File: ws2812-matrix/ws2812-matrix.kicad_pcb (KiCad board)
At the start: 2 copper layers, 80 x 80 mm, 270 parts, among them J1 Conn_01x03, J2 Conn_01x03

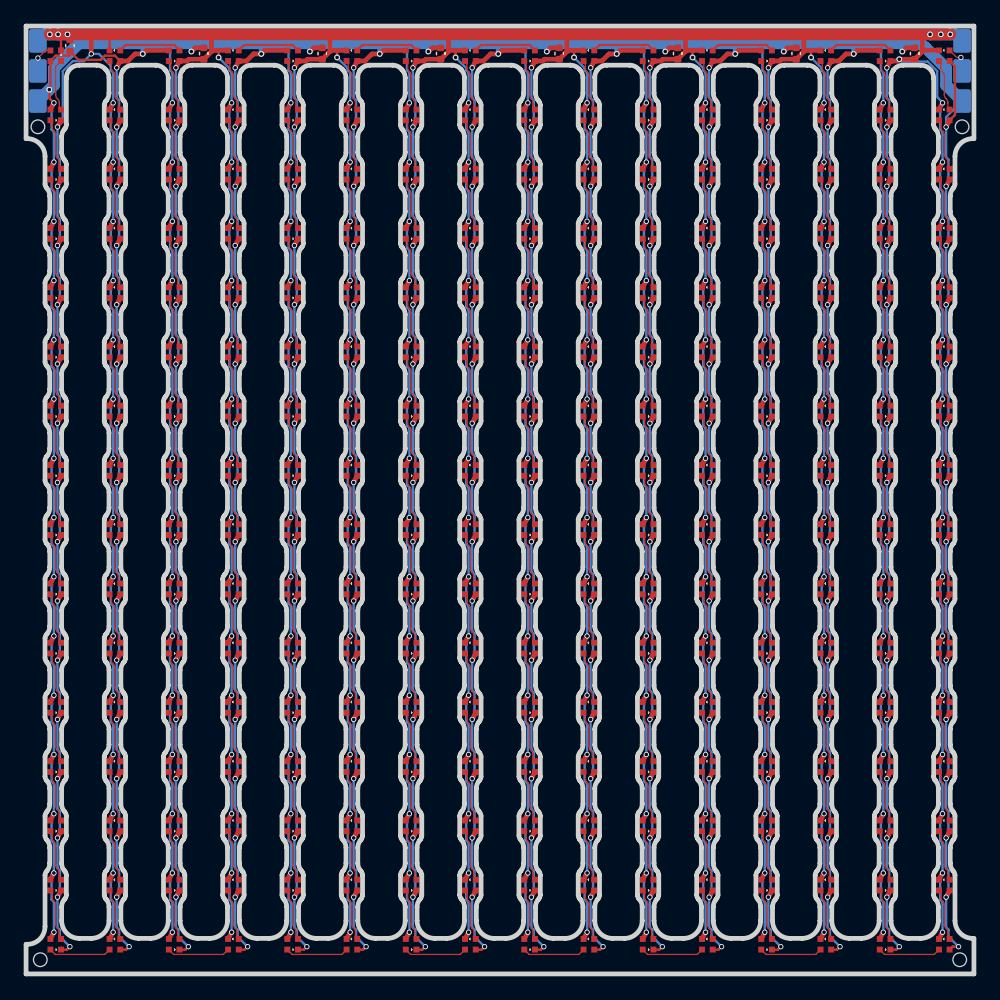
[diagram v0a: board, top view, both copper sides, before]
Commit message: ws2812-matrix: new attempt with more connections
Hopefully this'll go through JLCPCB review.
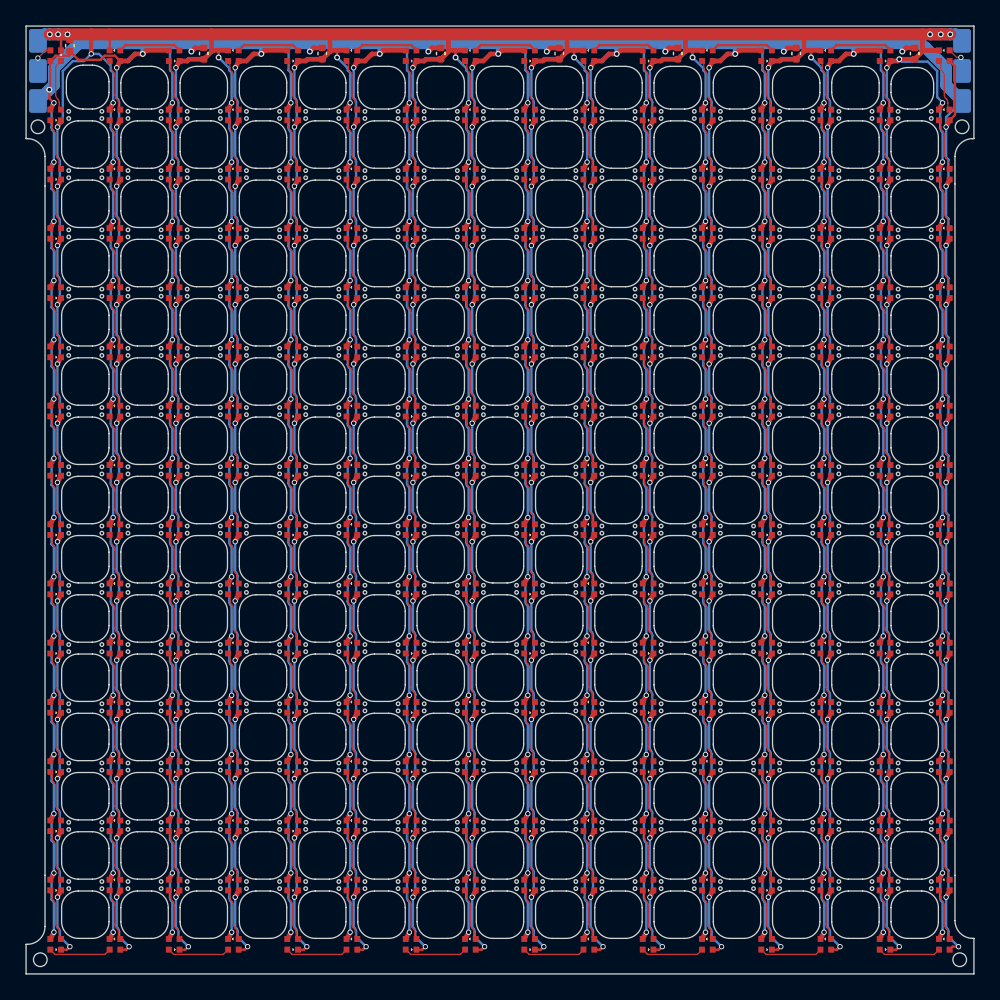
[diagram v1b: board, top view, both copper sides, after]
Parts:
- added REF**: BreakawayHole, Custom:BreakawayHole, F.Cu at (51.1, 54.7)
- added REF**: BreakawayHole, Custom:BreakawayHole, F.Cu at (51.1, 55.3)
- added REF**: BreakawayHole, Custom:BreakawayHole, F.Cu at (53.9, 55.3)
- added REF**: BreakawayHole, Custom:BreakawayHole, F.Cu at (51.1, 60.3)
- added REF**: BreakawayHole, Custom:BreakawayHole, F.Cu at (53.9, 54.7)
- added REF**: BreakawayHole, Custom:BreakawayHole, F.Cu at (53.9, 60.3)
- added REF**: BreakawayHole, Custom:BreakawayHole, F.Cu at (51.1, 59.7)
- added REF**: BreakawayHole, Custom:BreakawayHole, F.Cu at (53.9, 59.7)
- added REF**1: BreakawayHole, Custom:BreakawayHole, F.Cu at (56.1, 60.3)
- added REF**10: BreakawayHole, Custom:BreakawayHole, F.Cu at (76.1, 59.7)
- added REF**100: BreakawayHole, Custom:BreakawayHole, F.Cu at (76.1, 74.7)
- added REF**101: BreakawayHole, Custom:BreakawayHole, F.Cu at (81.1, 75.3)
- added REF**102: BreakawayHole, Custom:BreakawayHole, F.Cu at (81.1, 74.7)
- added REF**103: BreakawayHole, Custom:BreakawayHole, F.Cu at (86.1, 75.3)
- added REF**104: BreakawayHole, Custom:BreakawayHole, F.Cu at (86.1, 74.7)
- added REF**105: BreakawayHole, Custom:BreakawayHole, F.Cu at (91.1, 75.3)
- added REF**106: BreakawayHole, Custom:BreakawayHole, F.Cu at (91.1, 74.7)
- added REF**107: BreakawayHole, Custom:BreakawayHole, F.Cu at (96.1, 75.3)
- added REF**108: BreakawayHole, Custom:BreakawayHole, F.Cu at (96.1, 74.7)
- added REF**109: BreakawayHole, Custom:BreakawayHole, F.Cu at (101.1, 75.3)
- added REF**11: BreakawayHole, Custom:BreakawayHole, F.Cu at (81.1, 60.3)
- added REF**110: BreakawayHole, Custom:BreakawayHole, F.Cu at (101.1, 74.7)
- added REF**111: BreakawayHole, Custom:BreakawayHole, F.Cu at (106.1, 75.3)
- added REF**112: BreakawayHole, Custom:BreakawayHole, F.Cu at (106.1, 74.7)
- added REF**113: BreakawayHole, Custom:BreakawayHole, F.Cu at (111.1, 75.3)
- added REF**114: BreakawayHole, Custom:BreakawayHole, F.Cu at (111.1, 74.7)
- added REF**115: BreakawayHole, Custom:BreakawayHole, F.Cu at (116.1, 75.3)
- added REF**116: BreakawayHole, Custom:BreakawayHole, F.Cu at (116.1, 74.7)
- added REF**117: BreakawayHole, Custom:BreakawayHole, F.Cu at (121.1, 75.3)
- added REF**118: BreakawayHole, Custom:BreakawayHole, F.Cu at (121.1, 74.7)
- added REF**119: BreakawayHole, Custom:BreakawayHole, F.Cu at (51.1, 80.3)
- added REF**12: BreakawayHole, Custom:BreakawayHole, F.Cu at (81.1, 59.7)
- added REF**120: BreakawayHole, Custom:BreakawayHole, F.Cu at (51.1, 79.7)
- added REF**121: BreakawayHole, Custom:BreakawayHole, F.Cu at (56.1, 80.3)
- added REF**122: BreakawayHole, Custom:BreakawayHole, F.Cu at (56.1, 79.7)
- added REF**123: BreakawayHole, Custom:BreakawayHole, F.Cu at (61.1, 80.3)
- added REF**124: BreakawayHole, Custom:BreakawayHole, F.Cu at (61.1, 79.7)
- added REF**125: BreakawayHole, Custom:BreakawayHole, F.Cu at (66.1, 80.3)
- added REF**126: BreakawayHole, Custom:BreakawayHole, F.Cu at (66.1, 79.7)
- added REF**127: BreakawayHole, Custom:BreakawayHole, F.Cu at (71.1, 80.3)
- added REF**128: BreakawayHole, Custom:BreakawayHole, F.Cu at (71.1, 79.7)
- added REF**129: BreakawayHole, Custom:BreakawayHole, F.Cu at (76.1, 80.3)
- added REF**13: BreakawayHole, Custom:BreakawayHole, F.Cu at (86.1, 60.3)
- added REF**130: BreakawayHole, Custom:BreakawayHole, F.Cu at (76.1, 79.7)
- added REF**131: BreakawayHole, Custom:BreakawayHole, F.Cu at (81.1, 80.3)
- added REF**132: BreakawayHole, Custom:BreakawayHole, F.Cu at (81.1, 79.7)
- added REF**133: BreakawayHole, Custom:BreakawayHole, F.Cu at (86.1, 80.3)
- added REF**134: BreakawayHole, Custom:BreakawayHole, F.Cu at (86.1, 79.7)
- added REF**135: BreakawayHole, Custom:BreakawayHole, F.Cu at (91.1, 80.3)
- added REF**136: BreakawayHole, Custom:BreakawayHole, F.Cu at (91.1, 79.7)
- added REF**137: BreakawayHole, Custom:BreakawayHole, F.Cu at (96.1, 80.3)
- added REF**138: BreakawayHole, Custom:BreakawayHole, F.Cu at (96.1, 79.7)
- added REF**139: BreakawayHole, Custom:BreakawayHole, F.Cu at (101.1, 80.3)
- added REF**14: BreakawayHole, Custom:BreakawayHole, F.Cu at (86.1, 59.7)
- added REF**140: BreakawayHole, Custom:BreakawayHole, F.Cu at (101.1, 79.7)
- added REF**141: BreakawayHole, Custom:BreakawayHole, F.Cu at (106.1, 80.3)
- added REF**142: BreakawayHole, Custom:BreakawayHole, F.Cu at (106.1, 79.7)
- added REF**143: BreakawayHole, Custom:BreakawayHole, F.Cu at (111.1, 80.3)
- added REF**144: BreakawayHole, Custom:BreakawayHole, F.Cu at (111.1, 79.7)
- added REF**145: BreakawayHole, Custom:BreakawayHole, F.Cu at (116.1, 80.3)
- added REF**146: BreakawayHole, Custom:BreakawayHole, F.Cu at (116.1, 79.7)
- added REF**147: BreakawayHole, Custom:BreakawayHole, F.Cu at (121.1, 80.3)
- added REF**148: BreakawayHole, Custom:BreakawayHole, F.Cu at (121.1, 79.7)
- added REF**149: BreakawayHole, Custom:BreakawayHole, F.Cu at (51.1, 85.3)
- added REF**15: BreakawayHole, Custom:BreakawayHole, F.Cu at (91.1, 60.3)
- added REF**150: BreakawayHole, Custom:BreakawayHole, F.Cu at (51.1, 84.7)
- added REF**151: BreakawayHole, Custom:BreakawayHole, F.Cu at (56.1, 85.3)
- added REF**152: BreakawayHole, Custom:BreakawayHole, F.Cu at (56.1, 84.7)
- added REF**153: BreakawayHole, Custom:BreakawayHole, F.Cu at (61.1, 85.3)
- added REF**154: BreakawayHole, Custom:BreakawayHole, F.Cu at (61.1, 84.7)
- added REF**155: BreakawayHole, Custom:BreakawayHole, F.Cu at (66.1, 85.3)
- added REF**156: BreakawayHole, Custom:BreakawayHole, F.Cu at (66.1, 84.7)
- added REF**157: BreakawayHole, Custom:BreakawayHole, F.Cu at (71.1, 85.3)
- added REF**158: BreakawayHole, Custom:BreakawayHole, F.Cu at (71.1, 84.7)
- added REF**159: BreakawayHole, Custom:BreakawayHole, F.Cu at (76.1, 85.3)
- added REF**16: BreakawayHole, Custom:BreakawayHole, F.Cu at (91.1, 59.7)
- added REF**160: BreakawayHole, Custom:BreakawayHole, F.Cu at (76.1, 84.7)
- added REF**161: BreakawayHole, Custom:BreakawayHole, F.Cu at (81.1, 85.3)
- added REF**162: BreakawayHole, Custom:BreakawayHole, F.Cu at (81.1, 84.7)
- added REF**163: BreakawayHole, Custom:BreakawayHole, F.Cu at (86.1, 85.3)
- added REF**164: BreakawayHole, Custom:BreakawayHole, F.Cu at (86.1, 84.7)
- added REF**165: BreakawayHole, Custom:BreakawayHole, F.Cu at (91.1, 85.3)
- added REF**166: BreakawayHole, Custom:BreakawayHole, F.Cu at (91.1, 84.7)
- added REF**167: BreakawayHole, Custom:BreakawayHole, F.Cu at (96.1, 85.3)
- added REF**168: BreakawayHole, Custom:BreakawayHole, F.Cu at (96.1, 84.7)
- added REF**169: BreakawayHole, Custom:BreakawayHole, F.Cu at (101.1, 85.3)
- added REF**17: BreakawayHole, Custom:BreakawayHole, F.Cu at (96.1, 60.3)
- added REF**170: BreakawayHole, Custom:BreakawayHole, F.Cu at (101.1, 84.7)
- added REF**171: BreakawayHole, Custom:BreakawayHole, F.Cu at (106.1, 85.3)
- added REF**172: BreakawayHole, Custom:BreakawayHole, F.Cu at (106.1, 84.7)
- added REF**173: BreakawayHole, Custom:BreakawayHole, F.Cu at (111.1, 85.3)
- added REF**174: BreakawayHole, Custom:BreakawayHole, F.Cu at (111.1, 84.7)
- added REF**175: BreakawayHole, Custom:BreakawayHole, F.Cu at (116.1, 85.3)
- added REF**176: BreakawayHole, Custom:BreakawayHole, F.Cu at (116.1, 84.7)
- added REF**177: BreakawayHole, Custom:BreakawayHole, F.Cu at (121.1, 85.3)
- added REF**178: BreakawayHole, Custom:BreakawayHole, F.Cu at (121.1, 84.7)
- added REF**179: BreakawayHole, Custom:BreakawayHole, F.Cu at (51.1, 90.3)
- added REF**18: BreakawayHole, Custom:BreakawayHole, F.Cu at (96.1, 59.7)
- added REF**180: BreakawayHole, Custom:BreakawayHole, F.Cu at (51.1, 89.7)
- added REF**181: BreakawayHole, Custom:BreakawayHole, F.Cu at (56.1, 90.3)
- added REF**182: BreakawayHole, Custom:BreakawayHole, F.Cu at (56.1, 89.7)
- added REF**183: BreakawayHole, Custom:BreakawayHole, F.Cu at (61.1, 90.3)
- added REF**184: BreakawayHole, Custom:BreakawayHole, F.Cu at (61.1, 89.7)
- added REF**185: BreakawayHole, Custom:BreakawayHole, F.Cu at (66.1, 90.3)
- added REF**186: BreakawayHole, Custom:BreakawayHole, F.Cu at (66.1, 89.7)
- added REF**187: BreakawayHole, Custom:BreakawayHole, F.Cu at (71.1, 90.3)
- added REF**188: BreakawayHole, Custom:BreakawayHole, F.Cu at (71.1, 89.7)
- added REF**189: BreakawayHole, Custom:BreakawayHole, F.Cu at (76.1, 90.3)
- added REF**19: BreakawayHole, Custom:BreakawayHole, F.Cu at (101.1, 60.3)
- added REF**190: BreakawayHole, Custom:BreakawayHole, F.Cu at (76.1, 89.7)
- added REF**191: BreakawayHole, Custom:BreakawayHole, F.Cu at (81.1, 90.3)
- added REF**192: BreakawayHole, Custom:BreakawayHole, F.Cu at (81.1, 89.7)
- added REF**193: BreakawayHole, Custom:BreakawayHole, F.Cu at (86.1, 90.3)
- added REF**194: BreakawayHole, Custom:BreakawayHole, F.Cu at (86.1, 89.7)
- added REF**195: BreakawayHole, Custom:BreakawayHole, F.Cu at (91.1, 90.3)
- added REF**196: BreakawayHole, Custom:BreakawayHole, F.Cu at (91.1, 89.7)
- added REF**197: BreakawayHole, Custom:BreakawayHole, F.Cu at (96.1, 90.3)
- added REF**198: BreakawayHole, Custom:BreakawayHole, F.Cu at (96.1, 89.7)
- added REF**199: BreakawayHole, Custom:BreakawayHole, F.Cu at (101.1, 90.3)
- added REF**2: BreakawayHole, Custom:BreakawayHole, F.Cu at (56.1, 59.7)
- added REF**20: BreakawayHole, Custom:BreakawayHole, F.Cu at (101.1, 59.7)
- added REF**200: BreakawayHole, Custom:BreakawayHole, F.Cu at (101.1, 89.7)
- added REF**201: BreakawayHole, Custom:BreakawayHole, F.Cu at (106.1, 90.3)
- added REF**202: BreakawayHole, Custom:BreakawayHole, F.Cu at (106.1, 89.7)
- added REF**203: BreakawayHole, Custom:BreakawayHole, F.Cu at (111.1, 90.3)
- added REF**204: BreakawayHole, Custom:BreakawayHole, F.Cu at (111.1, 89.7)
- added REF**205: BreakawayHole, Custom:BreakawayHole, F.Cu at (116.1, 90.3)
- added REF**206: BreakawayHole, Custom:BreakawayHole, F.Cu at (116.1, 89.7)
- added REF**207: BreakawayHole, Custom:BreakawayHole, F.Cu at (121.1, 90.3)
- added REF**208: BreakawayHole, Custom:BreakawayHole, F.Cu at (121.1, 89.7)
- added REF**209: BreakawayHole, Custom:BreakawayHole, F.Cu at (51.1, 95.3)
- added REF**21: BreakawayHole, Custom:BreakawayHole, F.Cu at (106.1, 60.3)
- added REF**210: BreakawayHole, Custom:BreakawayHole, F.Cu at (51.1, 94.7)
- added REF**211: BreakawayHole, Custom:BreakawayHole, F.Cu at (56.1, 95.3)
- added REF**212: BreakawayHole, Custom:BreakawayHole, F.Cu at (56.1, 94.7)
- added REF**213: BreakawayHole, Custom:BreakawayHole, F.Cu at (61.1, 95.3)
- added REF**214: BreakawayHole, Custom:BreakawayHole, F.Cu at (61.1, 94.7)
- added REF**215: BreakawayHole, Custom:BreakawayHole, F.Cu at (66.1, 95.3)
- added REF**216: BreakawayHole, Custom:BreakawayHole, F.Cu at (66.1, 94.7)
- added REF**217: BreakawayHole, Custom:BreakawayHole, F.Cu at (71.1, 95.3)
- added REF**218: BreakawayHole, Custom:BreakawayHole, F.Cu at (71.1, 94.7)
- added REF**219: BreakawayHole, Custom:BreakawayHole, F.Cu at (76.1, 95.3)
- added REF**22: BreakawayHole, Custom:BreakawayHole, F.Cu at (106.1, 59.7)
- added REF**220: BreakawayHole, Custom:BreakawayHole, F.Cu at (76.1, 94.7)
- added REF**221: BreakawayHole, Custom:BreakawayHole, F.Cu at (81.1, 95.3)
- added REF**222: BreakawayHole, Custom:BreakawayHole, F.Cu at (81.1, 94.7)
- added REF**223: BreakawayHole, Custom:BreakawayHole, F.Cu at (86.1, 95.3)
- added REF**224: BreakawayHole, Custom:BreakawayHole, F.Cu at (86.1, 94.7)
- added REF**225: BreakawayHole, Custom:BreakawayHole, F.Cu at (91.1, 95.3)
- added REF**226: BreakawayHole, Custom:BreakawayHole, F.Cu at (91.1, 94.7)
- added REF**227: BreakawayHole, Custom:BreakawayHole, F.Cu at (96.1, 95.3)
- added REF**228: BreakawayHole, Custom:BreakawayHole, F.Cu at (96.1, 94.7)
- added REF**229: BreakawayHole, Custom:BreakawayHole, F.Cu at (101.1, 95.3)
- added REF**23: BreakawayHole, Custom:BreakawayHole, F.Cu at (111.1, 60.3)
- added REF**230: BreakawayHole, Custom:BreakawayHole, F.Cu at (101.1, 94.7)
- added REF**231: BreakawayHole, Custom:BreakawayHole, F.Cu at (106.1, 95.3)
- added REF**232: BreakawayHole, Custom:BreakawayHole, F.Cu at (106.1, 94.7)
- added REF**233: BreakawayHole, Custom:BreakawayHole, F.Cu at (111.1, 95.3)
- added REF**234: BreakawayHole, Custom:BreakawayHole, F.Cu at (111.1, 94.7)
- added REF**235: BreakawayHole, Custom:BreakawayHole, F.Cu at (116.1, 95.3)
- added REF**236: BreakawayHole, Custom:BreakawayHole, F.Cu at (116.1, 94.7)
- added REF**237: BreakawayHole, Custom:BreakawayHole, F.Cu at (121.1, 95.3)
- added REF**238: BreakawayHole, Custom:BreakawayHole, F.Cu at (121.1, 94.7)
- added REF**239: BreakawayHole, Custom:BreakawayHole, F.Cu at (51.1, 100.3)
- added REF**24: BreakawayHole, Custom:BreakawayHole, F.Cu at (111.1, 59.7)
- added REF**240: BreakawayHole, Custom:BreakawayHole, F.Cu at (51.1, 99.7)
- added REF**241: BreakawayHole, Custom:BreakawayHole, F.Cu at (56.1, 100.3)
- added REF**242: BreakawayHole, Custom:BreakawayHole, F.Cu at (56.1, 99.7)
- added REF**243: BreakawayHole, Custom:BreakawayHole, F.Cu at (61.1, 100.3)
- added REF**244: BreakawayHole, Custom:BreakawayHole, F.Cu at (61.1, 99.7)
- added REF**245: BreakawayHole, Custom:BreakawayHole, F.Cu at (66.1, 100.3)
- added REF**246: BreakawayHole, Custom:BreakawayHole, F.Cu at (66.1, 99.7)
- added REF**247: BreakawayHole, Custom:BreakawayHole, F.Cu at (71.1, 100.3)
- added REF**248: BreakawayHole, Custom:BreakawayHole, F.Cu at (71.1, 99.7)
- added REF**249: BreakawayHole, Custom:BreakawayHole, F.Cu at (76.1, 100.3)
- added REF**25: BreakawayHole, Custom:BreakawayHole, F.Cu at (116.1, 60.3)
- added REF**250: BreakawayHole, Custom:BreakawayHole, F.Cu at (76.1, 99.7)
- added REF**251: BreakawayHole, Custom:BreakawayHole, F.Cu at (81.1, 100.3)
- added REF**252: BreakawayHole, Custom:BreakawayHole, F.Cu at (81.1, 99.7)
- added REF**253: BreakawayHole, Custom:BreakawayHole, F.Cu at (86.1, 100.3)
- added REF**254: BreakawayHole, Custom:BreakawayHole, F.Cu at (86.1, 99.7)
- added REF**255: BreakawayHole, Custom:BreakawayHole, F.Cu at (91.1, 100.3)
- added REF**256: BreakawayHole, Custom:BreakawayHole, F.Cu at (91.1, 99.7)
- added REF**257: BreakawayHole, Custom:BreakawayHole, F.Cu at (96.1, 100.3)
- added REF**258: BreakawayHole, Custom:BreakawayHole, F.Cu at (96.1, 99.7)
- added REF**259: BreakawayHole, Custom:BreakawayHole, F.Cu at (101.1, 100.3)
- added REF**26: BreakawayHole, Custom:BreakawayHole, F.Cu at (116.1, 59.7)
- added REF**260: BreakawayHole, Custom:BreakawayHole, F.Cu at (101.1, 99.7)
- added REF**261: BreakawayHole, Custom:BreakawayHole, F.Cu at (106.1, 100.3)
- added REF**262: BreakawayHole, Custom:BreakawayHole, F.Cu at (106.1, 99.7)
- added REF**263: BreakawayHole, Custom:BreakawayHole, F.Cu at (111.1, 100.3)
- added REF**264: BreakawayHole, Custom:BreakawayHole, F.Cu at (111.1, 99.7)
- added REF**265: BreakawayHole, Custom:BreakawayHole, F.Cu at (116.1, 100.3)
- added REF**266: BreakawayHole, Custom:BreakawayHole, F.Cu at (116.1, 99.7)
- added REF**267: BreakawayHole, Custom:BreakawayHole, F.Cu at (121.1, 100.3)
- added REF**268: BreakawayHole, Custom:BreakawayHole, F.Cu at (121.1, 99.7)
- added REF**269: BreakawayHole, Custom:BreakawayHole, F.Cu at (51.1, 105.3)
- added REF**27: BreakawayHole, Custom:BreakawayHole, F.Cu at (121.1, 60.3)
- added REF**270: BreakawayHole, Custom:BreakawayHole, F.Cu at (51.1, 104.7)
- added REF**271: BreakawayHole, Custom:BreakawayHole, F.Cu at (56.1, 105.3)
- added REF**272: BreakawayHole, Custom:BreakawayHole, F.Cu at (56.1, 104.7)
- added REF**273: BreakawayHole, Custom:BreakawayHole, F.Cu at (61.1, 105.3)
- added REF**274: BreakawayHole, Custom:BreakawayHole, F.Cu at (61.1, 104.7)
- added REF**275: BreakawayHole, Custom:BreakawayHole, F.Cu at (66.1, 105.3)
- added REF**276: BreakawayHole, Custom:BreakawayHole, F.Cu at (66.1, 104.7)
- added REF**277: BreakawayHole, Custom:BreakawayHole, F.Cu at (71.1, 105.3)
- added REF**278: BreakawayHole, Custom:BreakawayHole, F.Cu at (71.1, 104.7)
- added REF**279: BreakawayHole, Custom:BreakawayHole, F.Cu at (76.1, 105.3)
- added REF**28: BreakawayHole, Custom:BreakawayHole, F.Cu at (121.1, 59.7)
- added REF**280: BreakawayHole, Custom:BreakawayHole, F.Cu at (76.1, 104.7)
- added REF**281: BreakawayHole, Custom:BreakawayHole, F.Cu at (81.1, 105.3)
- added REF**282: BreakawayHole, Custom:BreakawayHole, F.Cu at (81.1, 104.7)
- added REF**283: BreakawayHole, Custom:BreakawayHole, F.Cu at (86.1, 105.3)
- added REF**284: BreakawayHole, Custom:BreakawayHole, F.Cu at (86.1, 104.7)
- added REF**285: BreakawayHole, Custom:BreakawayHole, F.Cu at (91.1, 105.3)
- added REF**286: BreakawayHole, Custom:BreakawayHole, F.Cu at (91.1, 104.7)
- added REF**287: BreakawayHole, Custom:BreakawayHole, F.Cu at (96.1, 105.3)
- added REF**288: BreakawayHole, Custom:BreakawayHole, F.Cu at (96.1, 104.7)
- added REF**289: BreakawayHole, Custom:BreakawayHole, F.Cu at (101.1, 105.3)
- added REF**29: BreakawayHole, Custom:BreakawayHole, F.Cu at (51.1, 65.3)
- added REF**290: BreakawayHole, Custom:BreakawayHole, F.Cu at (101.1, 104.7)
- added REF**291: BreakawayHole, Custom:BreakawayHole, F.Cu at (106.1, 105.3)
- added REF**292: BreakawayHole, Custom:BreakawayHole, F.Cu at (106.1, 104.7)
- added REF**293: BreakawayHole, Custom:BreakawayHole, F.Cu at (111.1, 105.3)
- added REF**294: BreakawayHole, Custom:BreakawayHole, F.Cu at (111.1, 104.7)
- added REF**295: BreakawayHole, Custom:BreakawayHole, F.Cu at (116.1, 105.3)
- added REF**296: BreakawayHole, Custom:BreakawayHole, F.Cu at (116.1, 104.7)
- added REF**297: BreakawayHole, Custom:BreakawayHole, F.Cu at (121.1, 105.3)
- added REF**298: BreakawayHole, Custom:BreakawayHole, F.Cu at (121.1, 104.7)
- added REF**299: BreakawayHole, Custom:BreakawayHole, F.Cu at (51.1, 110.3)
- added REF**3: BreakawayHole, Custom:BreakawayHole, F.Cu at (61.1, 60.3)
- added REF**30: BreakawayHole, Custom:BreakawayHole, F.Cu at (51.1, 64.7)
- added REF**300: BreakawayHole, Custom:BreakawayHole, F.Cu at (51.1, 109.7)
- added REF**301: BreakawayHole, Custom:BreakawayHole, F.Cu at (56.1, 110.3)
- added REF**302: BreakawayHole, Custom:BreakawayHole, F.Cu at (56.1, 109.7)
- added REF**303: BreakawayHole, Custom:BreakawayHole, F.Cu at (61.1, 110.3)
- added REF**304: BreakawayHole, Custom:BreakawayHole, F.Cu at (61.1, 109.7)
- added REF**305: BreakawayHole, Custom:BreakawayHole, F.Cu at (66.1, 110.3)
- added REF**306: BreakawayHole, Custom:BreakawayHole, F.Cu at (66.1, 109.7)
- added REF**307: BreakawayHole, Custom:BreakawayHole, F.Cu at (71.1, 110.3)
- added REF**308: BreakawayHole, Custom:BreakawayHole, F.Cu at (71.1, 109.7)
- added REF**309: BreakawayHole, Custom:BreakawayHole, F.Cu at (76.1, 110.3)
- added REF**31: BreakawayHole, Custom:BreakawayHole, F.Cu at (56.1, 65.3)
- added REF**310: BreakawayHole, Custom:BreakawayHole, F.Cu at (76.1, 109.7)
- added REF**311: BreakawayHole, Custom:BreakawayHole, F.Cu at (81.1, 110.3)
- added REF**312: BreakawayHole, Custom:BreakawayHole, F.Cu at (81.1, 109.7)
- added REF**313: BreakawayHole, Custom:BreakawayHole, F.Cu at (86.1, 110.3)
- added REF**314: BreakawayHole, Custom:BreakawayHole, F.Cu at (86.1, 109.7)
- added REF**315: BreakawayHole, Custom:BreakawayHole, F.Cu at (91.1, 110.3)
- added REF**316: BreakawayHole, Custom:BreakawayHole, F.Cu at (91.1, 109.7)
- added REF**317: BreakawayHole, Custom:BreakawayHole, F.Cu at (96.1, 110.3)
- added REF**318: BreakawayHole, Custom:BreakawayHole, F.Cu at (96.1, 109.7)
- added REF**319: BreakawayHole, Custom:BreakawayHole, F.Cu at (101.1, 110.3)
- added REF**32: BreakawayHole, Custom:BreakawayHole, F.Cu at (56.1, 64.7)
- added REF**320: BreakawayHole, Custom:BreakawayHole, F.Cu at (101.1, 109.7)
- added REF**321: BreakawayHole, Custom:BreakawayHole, F.Cu at (106.1, 110.3)
- added REF**322: BreakawayHole, Custom:BreakawayHole, F.Cu at (106.1, 109.7)
- added REF**323: BreakawayHole, Custom:BreakawayHole, F.Cu at (111.1, 110.3)
- added REF**324: BreakawayHole, Custom:BreakawayHole, F.Cu at (111.1, 109.7)
- added REF**325: BreakawayHole, Custom:BreakawayHole, F.Cu at (116.1, 110.3)
- added REF**326: BreakawayHole, Custom:BreakawayHole, F.Cu at (116.1, 109.7)
- added REF**327: BreakawayHole, Custom:BreakawayHole, F.Cu at (121.1, 110.3)
- added REF**328: BreakawayHole, Custom:BreakawayHole, F.Cu at (121.1, 109.7)
- added REF**329: BreakawayHole, Custom:BreakawayHole, F.Cu at (51.1, 115.3)
- added REF**33: BreakawayHole, Custom:BreakawayHole, F.Cu at (61.1, 65.3)
- added REF**330: BreakawayHole, Custom:BreakawayHole, F.Cu at (51.1, 114.7)
- added REF**331: BreakawayHole, Custom:BreakawayHole, F.Cu at (56.1, 115.3)
- added REF**332: BreakawayHole, Custom:BreakawayHole, F.Cu at (56.1, 114.7)
- added REF**333: BreakawayHole, Custom:BreakawayHole, F.Cu at (61.1, 115.3)
- added REF**334: BreakawayHole, Custom:BreakawayHole, F.Cu at (61.1, 114.7)
- added REF**335: BreakawayHole, Custom:BreakawayHole, F.Cu at (66.1, 115.3)
- added REF**336: BreakawayHole, Custom:BreakawayHole, F.Cu at (66.1, 114.7)
- added REF**337: BreakawayHole, Custom:BreakawayHole, F.Cu at (71.1, 115.3)
- added REF**338: BreakawayHole, Custom:BreakawayHole, F.Cu at (71.1, 114.7)
- added REF**339: BreakawayHole, Custom:BreakawayHole, F.Cu at (76.1, 115.3)
- added REF**34: BreakawayHole, Custom:BreakawayHole, F.Cu at (61.1, 64.7)
- added REF**340: BreakawayHole, Custom:BreakawayHole, F.Cu at (76.1, 114.7)
- added REF**341: BreakawayHole, Custom:BreakawayHole, F.Cu at (81.1, 115.3)
- added REF**342: BreakawayHole, Custom:BreakawayHole, F.Cu at (81.1, 114.7)
- added REF**343: BreakawayHole, Custom:BreakawayHole, F.Cu at (86.1, 115.3)
- added REF**344: BreakawayHole, Custom:BreakawayHole, F.Cu at (86.1, 114.7)
- added REF**345: BreakawayHole, Custom:BreakawayHole, F.Cu at (91.1, 115.3)
- added REF**346: BreakawayHole, Custom:BreakawayHole, F.Cu at (91.1, 114.7)
- added REF**347: BreakawayHole, Custom:BreakawayHole, F.Cu at (96.1, 115.3)
- added REF**348: BreakawayHole, Custom:BreakawayHole, F.Cu at (96.1, 114.7)
- added REF**349: BreakawayHole, Custom:BreakawayHole, F.Cu at (101.1, 115.3)
- added REF**35: BreakawayHole, Custom:BreakawayHole, F.Cu at (66.1, 65.3)
- added REF**350: BreakawayHole, Custom:BreakawayHole, F.Cu at (101.1, 114.7)
- added REF**351: BreakawayHole, Custom:BreakawayHole, F.Cu at (106.1, 115.3)
- added REF**352: BreakawayHole, Custom:BreakawayHole, F.Cu at (106.1, 114.7)
- added REF**353: BreakawayHole, Custom:BreakawayHole, F.Cu at (111.1, 115.3)
- added REF**354: BreakawayHole, Custom:BreakawayHole, F.Cu at (111.1, 114.7)
- added REF**355: BreakawayHole, Custom:BreakawayHole, F.Cu at (116.1, 115.3)
- added REF**356: BreakawayHole, Custom:BreakawayHole, F.Cu at (116.1, 114.7)
- added REF**357: BreakawayHole, Custom:BreakawayHole, F.Cu at (121.1, 115.3)
- added REF**358: BreakawayHole, Custom:BreakawayHole, F.Cu at (121.1, 114.7)
- added REF**359: BreakawayHole, Custom:BreakawayHole, F.Cu at (51.1, 120.3)
- added REF**36: BreakawayHole, Custom:BreakawayHole, F.Cu at (66.1, 64.7)
- added REF**360: BreakawayHole, Custom:BreakawayHole, F.Cu at (51.1, 119.7)
- added REF**361: BreakawayHole, Custom:BreakawayHole, F.Cu at (56.1, 120.3)
- added REF**362: BreakawayHole, Custom:BreakawayHole, F.Cu at (56.1, 119.7)
- added REF**363: BreakawayHole, Custom:BreakawayHole, F.Cu at (61.1, 120.3)
- added REF**364: BreakawayHole, Custom:BreakawayHole, F.Cu at (61.1, 119.7)
- added REF**365: BreakawayHole, Custom:BreakawayHole, F.Cu at (66.1, 120.3)
- added REF**366: BreakawayHole, Custom:BreakawayHole, F.Cu at (66.1, 119.7)
- added REF**367: BreakawayHole, Custom:BreakawayHole, F.Cu at (71.1, 120.3)
- added REF**368: BreakawayHole, Custom:BreakawayHole, F.Cu at (71.1, 119.7)
- added REF**369: BreakawayHole, Custom:BreakawayHole, F.Cu at (76.1, 120.3)
- added REF**37: BreakawayHole, Custom:BreakawayHole, F.Cu at (71.1, 65.3)
- added REF**370: BreakawayHole, Custom:BreakawayHole, F.Cu at (76.1, 119.7)
- added REF**371: BreakawayHole, Custom:BreakawayHole, F.Cu at (81.1, 120.3)
- added REF**372: BreakawayHole, Custom:BreakawayHole, F.Cu at (81.1, 119.7)
- added REF**373: BreakawayHole, Custom:BreakawayHole, F.Cu at (86.1, 120.3)
- added REF**374: BreakawayHole, Custom:BreakawayHole, F.Cu at (86.1, 119.7)
- added REF**375: BreakawayHole, Custom:BreakawayHole, F.Cu at (91.1, 120.3)
- added REF**376: BreakawayHole, Custom:BreakawayHole, F.Cu at (91.1, 119.7)
- added REF**377: BreakawayHole, Custom:BreakawayHole, F.Cu at (96.1, 120.3)
- added REF**378: BreakawayHole, Custom:BreakawayHole, F.Cu at (96.1, 119.7)
- added REF**379: BreakawayHole, Custom:BreakawayHole, F.Cu at (101.1, 120.3)
- added REF**38: BreakawayHole, Custom:BreakawayHole, F.Cu at (71.1, 64.7)
- added REF**380: BreakawayHole, Custom:BreakawayHole, F.Cu at (101.1, 119.7)
- added REF**381: BreakawayHole, Custom:BreakawayHole, F.Cu at (106.1, 120.3)
- added REF**382: BreakawayHole, Custom:BreakawayHole, F.Cu at (106.1, 119.7)
- added REF**383: BreakawayHole, Custom:BreakawayHole, F.Cu at (111.1, 120.3)
- added REF**384: BreakawayHole, Custom:BreakawayHole, F.Cu at (111.1, 119.7)
- added REF**385: BreakawayHole, Custom:BreakawayHole, F.Cu at (116.1, 120.3)
- added REF**386: BreakawayHole, Custom:BreakawayHole, F.Cu at (116.1, 119.7)
- added REF**387: BreakawayHole, Custom:BreakawayHole, F.Cu at (121.1, 120.3)
- added REF**388: BreakawayHole, Custom:BreakawayHole, F.Cu at (121.1, 119.7)
- added REF**389: BreakawayHole, Custom:BreakawayHole, F.Cu at (58.9, 60.3)
- added REF**39: BreakawayHole, Custom:BreakawayHole, F.Cu at (76.1, 65.3)
- added REF**390: BreakawayHole, Custom:BreakawayHole, F.Cu at (58.9, 59.7)
- added REF**391: BreakawayHole, Custom:BreakawayHole, F.Cu at (63.9, 60.3)
- added REF**392: BreakawayHole, Custom:BreakawayHole, F.Cu at (63.9, 59.7)
- added REF**393: BreakawayHole, Custom:BreakawayHole, F.Cu at (68.9, 60.3)
- added REF**394: BreakawayHole, Custom:BreakawayHole, F.Cu at (68.9, 59.7)
- added REF**395: BreakawayHole, Custom:BreakawayHole, F.Cu at (73.9, 60.3)
- added REF**396: BreakawayHole, Custom:BreakawayHole, F.Cu at (73.9, 59.7)
- added REF**397: BreakawayHole, Custom:BreakawayHole, F.Cu at (78.9, 60.3)
- added REF**398: BreakawayHole, Custom:BreakawayHole, F.Cu at (78.9, 59.7)
- added REF**399: BreakawayHole, Custom:BreakawayHole, F.Cu at (83.9, 60.3)
- added REF**4: BreakawayHole, Custom:BreakawayHole, F.Cu at (61.1, 59.7)
- added REF**40: BreakawayHole, Custom:BreakawayHole, F.Cu at (76.1, 64.7)
- added REF**400: BreakawayHole, Custom:BreakawayHole, F.Cu at (83.9, 59.7)
- added REF**401: BreakawayHole, Custom:BreakawayHole, F.Cu at (88.9, 60.3)
- added REF**402: BreakawayHole, Custom:BreakawayHole, F.Cu at (88.9, 59.7)
- added REF**403: BreakawayHole, Custom:BreakawayHole, F.Cu at (93.9, 60.3)
- added REF**404: BreakawayHole, Custom:BreakawayHole, F.Cu at (93.9, 59.7)
- added REF**405: BreakawayHole, Custom:BreakawayHole, F.Cu at (98.9, 60.3)
- added REF**406: BreakawayHole, Custom:BreakawayHole, F.Cu at (98.9, 59.7)
- added REF**407: BreakawayHole, Custom:BreakawayHole, F.Cu at (103.9, 60.3)
- added REF**408: BreakawayHole, Custom:BreakawayHole, F.Cu at (103.9, 59.7)
- added REF**409: BreakawayHole, Custom:BreakawayHole, F.Cu at (108.9, 60.3)
- added REF**41: BreakawayHole, Custom:BreakawayHole, F.Cu at (81.1, 65.3)
- added REF**410: BreakawayHole, Custom:BreakawayHole, F.Cu at (108.9, 59.7)
- added REF**411: BreakawayHole, Custom:BreakawayHole, F.Cu at (113.9, 60.3)
- added REF**412: BreakawayHole, Custom:BreakawayHole, F.Cu at (113.9, 59.7)
- added REF**413: BreakawayHole, Custom:BreakawayHole, F.Cu at (118.9, 60.3)
- added REF**414: BreakawayHole, Custom:BreakawayHole, F.Cu at (118.9, 59.7)
- added REF**415: BreakawayHole, Custom:BreakawayHole, F.Cu at (123.9, 60.3)
- added REF**416: BreakawayHole, Custom:BreakawayHole, F.Cu at (123.9, 59.7)
- added REF**417: BreakawayHole, Custom:BreakawayHole, F.Cu at (53.9, 65.3)
- added REF**418: BreakawayHole, Custom:BreakawayHole, F.Cu at (53.9, 64.7)
- added REF**419: BreakawayHole, Custom:BreakawayHole, F.Cu at (58.9, 65.3)
- added REF**42: BreakawayHole, Custom:BreakawayHole, F.Cu at (81.1, 64.7)
- added REF**420: BreakawayHole, Custom:BreakawayHole, F.Cu at (58.9, 64.7)
- added REF**421: BreakawayHole, Custom:BreakawayHole, F.Cu at (63.9, 65.3)
- added REF**422: BreakawayHole, Custom:BreakawayHole, F.Cu at (63.9, 64.7)
- added REF**423: BreakawayHole, Custom:BreakawayHole, F.Cu at (68.9, 65.3)
- added REF**424: BreakawayHole, Custom:BreakawayHole, F.Cu at (68.9, 64.7)
- added REF**425: BreakawayHole, Custom:BreakawayHole, F.Cu at (73.9, 65.3)
- added REF**426: BreakawayHole, Custom:BreakawayHole, F.Cu at (73.9, 64.7)
- added REF**427: BreakawayHole, Custom:BreakawayHole, F.Cu at (78.9, 65.3)
- added REF**428: BreakawayHole, Custom:BreakawayHole, F.Cu at (78.9, 64.7)
- added REF**429: BreakawayHole, Custom:BreakawayHole, F.Cu at (83.9, 65.3)
- added REF**43: BreakawayHole, Custom:BreakawayHole, F.Cu at (86.1, 65.3)
- added REF**430: BreakawayHole, Custom:BreakawayHole, F.Cu at (83.9, 64.7)
- added REF**431: BreakawayHole, Custom:BreakawayHole, F.Cu at (88.9, 65.3)
- added REF**432: BreakawayHole, Custom:BreakawayHole, F.Cu at (88.9, 64.7)
- added REF**433: BreakawayHole, Custom:BreakawayHole, F.Cu at (93.9, 65.3)
- added REF**434: BreakawayHole, Custom:BreakawayHole, F.Cu at (93.9, 64.7)
- added REF**435: BreakawayHole, Custom:BreakawayHole, F.Cu at (98.9, 65.3)
- added REF**436: BreakawayHole, Custom:BreakawayHole, F.Cu at (98.9, 64.7)
- added REF**437: BreakawayHole, Custom:BreakawayHole, F.Cu at (103.9, 65.3)
- added REF**438: BreakawayHole, Custom:BreakawayHole, F.Cu at (103.9, 64.7)
- added REF**439: BreakawayHole, Custom:BreakawayHole, F.Cu at (108.9, 65.3)
- added REF**44: BreakawayHole, Custom:BreakawayHole, F.Cu at (86.1, 64.7)
- added REF**440: BreakawayHole, Custom:BreakawayHole, F.Cu at (108.9, 64.7)
- added REF**441: BreakawayHole, Custom:BreakawayHole, F.Cu at (113.9, 65.3)
- added REF**442: BreakawayHole, Custom:BreakawayHole, F.Cu at (113.9, 64.7)
- added REF**443: BreakawayHole, Custom:BreakawayHole, F.Cu at (118.9, 65.3)
- added REF**444: BreakawayHole, Custom:BreakawayHole, F.Cu at (118.9, 64.7)
- added REF**445: BreakawayHole, Custom:BreakawayHole, F.Cu at (123.9, 65.3)
- added REF**446: BreakawayHole, Custom:BreakawayHole, F.Cu at (123.9, 64.7)
- added REF**447: BreakawayHole, Custom:BreakawayHole, F.Cu at (53.9, 70.3)
- added REF**448: BreakawayHole, Custom:BreakawayHole, F.Cu at (53.9, 69.7)
- added REF**449: BreakawayHole, Custom:BreakawayHole, F.Cu at (58.9, 70.3)
- added REF**45: BreakawayHole, Custom:BreakawayHole, F.Cu at (91.1, 65.3)
- added REF**450: BreakawayHole, Custom:BreakawayHole, F.Cu at (58.9, 69.7)
- added REF**451: BreakawayHole, Custom:BreakawayHole, F.Cu at (63.9, 70.3)
- added REF**452: BreakawayHole, Custom:BreakawayHole, F.Cu at (63.9, 69.7)
- added REF**453: BreakawayHole, Custom:BreakawayHole, F.Cu at (68.9, 70.3)
- added REF**454: BreakawayHole, Custom:BreakawayHole, F.Cu at (68.9, 69.7)
- added REF**455: BreakawayHole, Custom:BreakawayHole, F.Cu at (73.9, 70.3)
- added REF**456: BreakawayHole, Custom:BreakawayHole, F.Cu at (73.9, 69.7)
- added REF**457: BreakawayHole, Custom:BreakawayHole, F.Cu at (78.9, 70.3)
- added REF**458: BreakawayHole, Custom:BreakawayHole, F.Cu at (78.9, 69.7)
- added REF**459: BreakawayHole, Custom:BreakawayHole, F.Cu at (83.9, 70.3)
- added REF**46: BreakawayHole, Custom:BreakawayHole, F.Cu at (91.1, 64.7)
- added REF**460: BreakawayHole, Custom:BreakawayHole, F.Cu at (83.9, 69.7)
- added REF**461: BreakawayHole, Custom:BreakawayHole, F.Cu at (88.9, 70.3)
- added REF**462: BreakawayHole, Custom:BreakawayHole, F.Cu at (88.9, 69.7)
- added REF**463: BreakawayHole, Custom:BreakawayHole, F.Cu at (93.9, 70.3)
- added REF**464: BreakawayHole, Custom:BreakawayHole, F.Cu at (93.9, 69.7)
- added REF**465: BreakawayHole, Custom:BreakawayHole, F.Cu at (98.9, 70.3)
- added REF**466: BreakawayHole, Custom:BreakawayHole, F.Cu at (98.9, 69.7)
- added REF**467: BreakawayHole, Custom:BreakawayHole, F.Cu at (103.9, 70.3)
- added REF**468: BreakawayHole, Custom:BreakawayHole, F.Cu at (103.9, 69.7)
- added REF**469: BreakawayHole, Custom:BreakawayHole, F.Cu at (108.9, 70.3)
- added REF**47: BreakawayHole, Custom:BreakawayHole, F.Cu at (96.1, 65.3)
- added REF**470: BreakawayHole, Custom:BreakawayHole, F.Cu at (108.9, 69.7)
- added REF**471: BreakawayHole, Custom:BreakawayHole, F.Cu at (113.9, 70.3)
- added REF**472: BreakawayHole, Custom:BreakawayHole, F.Cu at (113.9, 69.7)
- added REF**473: BreakawayHole, Custom:BreakawayHole, F.Cu at (118.9, 70.3)
- added REF**474: BreakawayHole, Custom:BreakawayHole, F.Cu at (118.9, 69.7)
- added REF**475: BreakawayHole, Custom:BreakawayHole, F.Cu at (123.9, 70.3)
- added REF**476: BreakawayHole, Custom:BreakawayHole, F.Cu at (123.9, 69.7)
- added REF**477: BreakawayHole, Custom:BreakawayHole, F.Cu at (53.9, 75.3)
- added REF**478: BreakawayHole, Custom:BreakawayHole, F.Cu at (53.9, 74.7)
- added REF**479: BreakawayHole, Custom:BreakawayHole, F.Cu at (58.9, 75.3)
- added REF**48: BreakawayHole, Custom:BreakawayHole, F.Cu at (96.1, 64.7)
- added REF**480: BreakawayHole, Custom:BreakawayHole, F.Cu at (58.9, 74.7)
- added REF**481: BreakawayHole, Custom:BreakawayHole, F.Cu at (63.9, 75.3)
- added REF**482: BreakawayHole, Custom:BreakawayHole, F.Cu at (63.9, 74.7)
- added REF**483: BreakawayHole, Custom:BreakawayHole, F.Cu at (68.9, 75.3)
- added REF**484: BreakawayHole, Custom:BreakawayHole, F.Cu at (68.9, 74.7)
- added REF**485: BreakawayHole, Custom:BreakawayHole, F.Cu at (73.9, 75.3)
- added REF**486: BreakawayHole, Custom:BreakawayHole, F.Cu at (73.9, 74.7)
- added REF**487: BreakawayHole, Custom:BreakawayHole, F.Cu at (78.9, 75.3)
- added REF**488: BreakawayHole, Custom:BreakawayHole, F.Cu at (78.9, 74.7)
- added REF**489: BreakawayHole, Custom:BreakawayHole, F.Cu at (83.9, 75.3)
- added REF**49: BreakawayHole, Custom:BreakawayHole, F.Cu at (101.1, 65.3)
- added REF**490: BreakawayHole, Custom:BreakawayHole, F.Cu at (83.9, 74.7)
- added REF**491: BreakawayHole, Custom:BreakawayHole, F.Cu at (88.9, 75.3)
- added REF**492: BreakawayHole, Custom:BreakawayHole, F.Cu at (88.9, 74.7)
- added REF**493: BreakawayHole, Custom:BreakawayHole, F.Cu at (93.9, 75.3)
- added REF**494: BreakawayHole, Custom:BreakawayHole, F.Cu at (93.9, 74.7)
- added REF**495: BreakawayHole, Custom:BreakawayHole, F.Cu at (98.9, 75.3)
- added REF**496: BreakawayHole, Custom:BreakawayHole, F.Cu at (98.9, 74.7)
- added REF**497: BreakawayHole, Custom:BreakawayHole, F.Cu at (103.9, 75.3)
- added REF**498: BreakawayHole, Custom:BreakawayHole, F.Cu at (103.9, 74.7)
- added REF**499: BreakawayHole, Custom:BreakawayHole, F.Cu at (108.9, 75.3)
- added REF**5: BreakawayHole, Custom:BreakawayHole, F.Cu at (66.1, 60.3)
- added REF**50: BreakawayHole, Custom:BreakawayHole, F.Cu at (101.1, 64.7)
- added REF**500: BreakawayHole, Custom:BreakawayHole, F.Cu at (108.9, 74.7)
- added REF**501: BreakawayHole, Custom:BreakawayHole, F.Cu at (113.9, 75.3)
- added REF**502: BreakawayHole, Custom:BreakawayHole, F.Cu at (113.9, 74.7)
- added REF**503: BreakawayHole, Custom:BreakawayHole, F.Cu at (118.9, 75.3)
- added REF**504: BreakawayHole, Custom:BreakawayHole, F.Cu at (118.9, 74.7)
- added REF**505: BreakawayHole, Custom:BreakawayHole, F.Cu at (123.9, 75.3)
- added REF**506: BreakawayHole, Custom:BreakawayHole, F.Cu at (123.9, 74.7)
- added REF**507: BreakawayHole, Custom:BreakawayHole, F.Cu at (53.9, 80.3)
- added REF**508: BreakawayHole, Custom:BreakawayHole, F.Cu at (53.9, 79.7)
- added REF**509: BreakawayHole, Custom:BreakawayHole, F.Cu at (58.9, 80.3)
- added REF**51: BreakawayHole, Custom:BreakawayHole, F.Cu at (106.1, 65.3)
- added REF**510: BreakawayHole, Custom:BreakawayHole, F.Cu at (58.9, 79.7)
- added REF**511: BreakawayHole, Custom:BreakawayHole, F.Cu at (63.9, 80.3)
- added REF**512: BreakawayHole, Custom:BreakawayHole, F.Cu at (63.9, 79.7)
- added REF**513: BreakawayHole, Custom:BreakawayHole, F.Cu at (68.9, 80.3)
- added REF**514: BreakawayHole, Custom:BreakawayHole, F.Cu at (68.9, 79.7)
- added REF**515: BreakawayHole, Custom:BreakawayHole, F.Cu at (73.9, 80.3)
- added REF**516: BreakawayHole, Custom:BreakawayHole, F.Cu at (73.9, 79.7)
- added REF**517: BreakawayHole, Custom:BreakawayHole, F.Cu at (78.9, 80.3)
- added REF**518: BreakawayHole, Custom:BreakawayHole, F.Cu at (78.9, 79.7)
- added REF**519: BreakawayHole, Custom:BreakawayHole, F.Cu at (83.9, 80.3)
- added REF**52: BreakawayHole, Custom:BreakawayHole, F.Cu at (106.1, 64.7)
- added REF**520: BreakawayHole, Custom:BreakawayHole, F.Cu at (83.9, 79.7)
- added REF**521: BreakawayHole, Custom:BreakawayHole, F.Cu at (88.9, 80.3)
- added REF**522: BreakawayHole, Custom:BreakawayHole, F.Cu at (88.9, 79.7)
- added REF**523: BreakawayHole, Custom:BreakawayHole, F.Cu at (93.9, 80.3)
- added REF**524: BreakawayHole, Custom:BreakawayHole, F.Cu at (93.9, 79.7)
- added REF**525: BreakawayHole, Custom:BreakawayHole, F.Cu at (98.9, 80.3)
- added REF**526: BreakawayHole, Custom:BreakawayHole, F.Cu at (98.9, 79.7)
- added REF**527: BreakawayHole, Custom:BreakawayHole, F.Cu at (103.9, 80.3)
- added REF**528: BreakawayHole, Custom:BreakawayHole, F.Cu at (103.9, 79.7)
- added REF**529: BreakawayHole, Custom:BreakawayHole, F.Cu at (108.9, 80.3)
- added REF**53: BreakawayHole, Custom:BreakawayHole, F.Cu at (111.1, 65.3)
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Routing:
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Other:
- outline, holes or cut-outs redrawn
